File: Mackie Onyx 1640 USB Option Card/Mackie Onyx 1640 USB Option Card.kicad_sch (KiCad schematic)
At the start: 0 parts

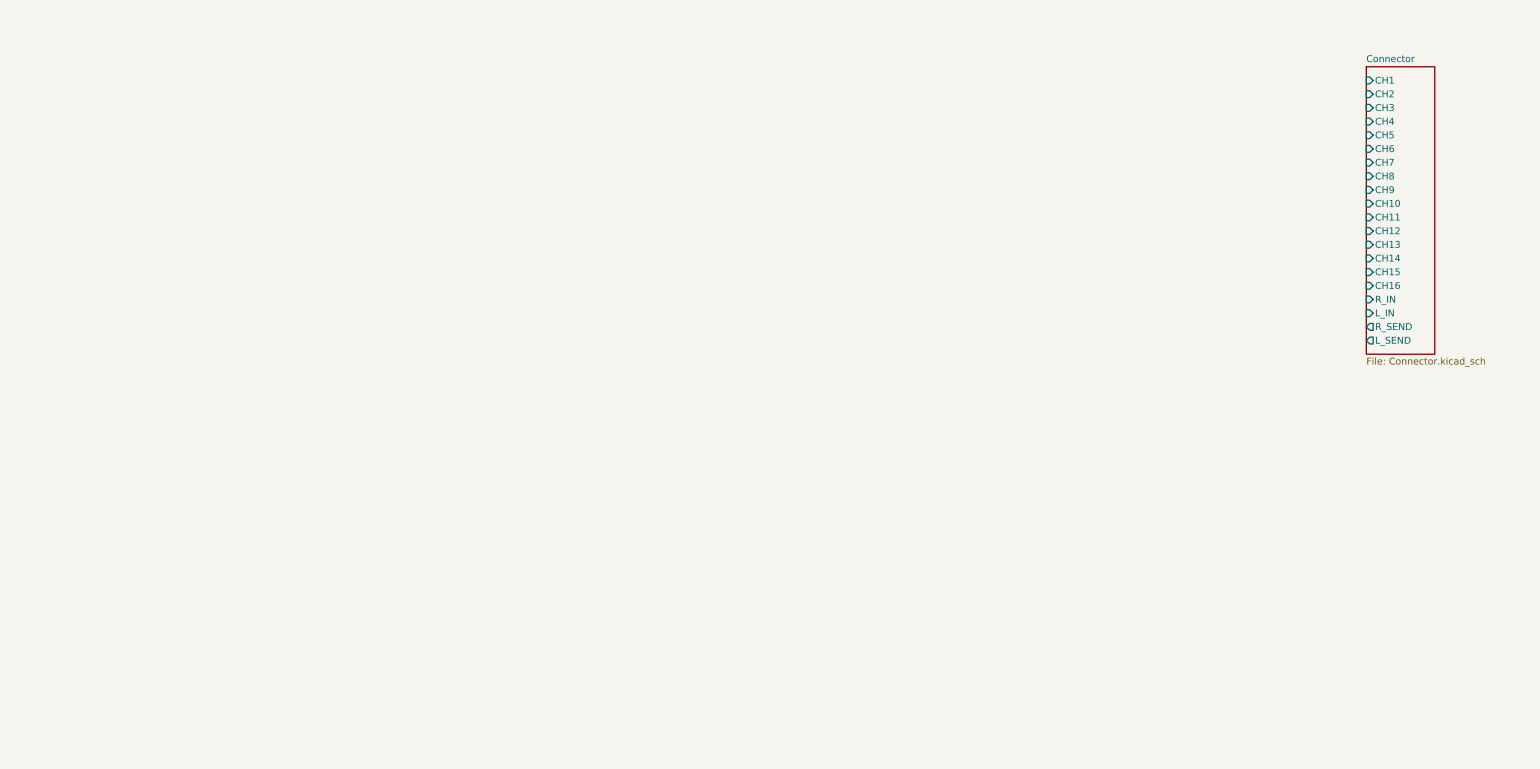
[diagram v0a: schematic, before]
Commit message: added XMOS XU316-1024-QF60B-C24 MCU (following footprint in pcb) started MCU power and usb phy implementation following datasheet
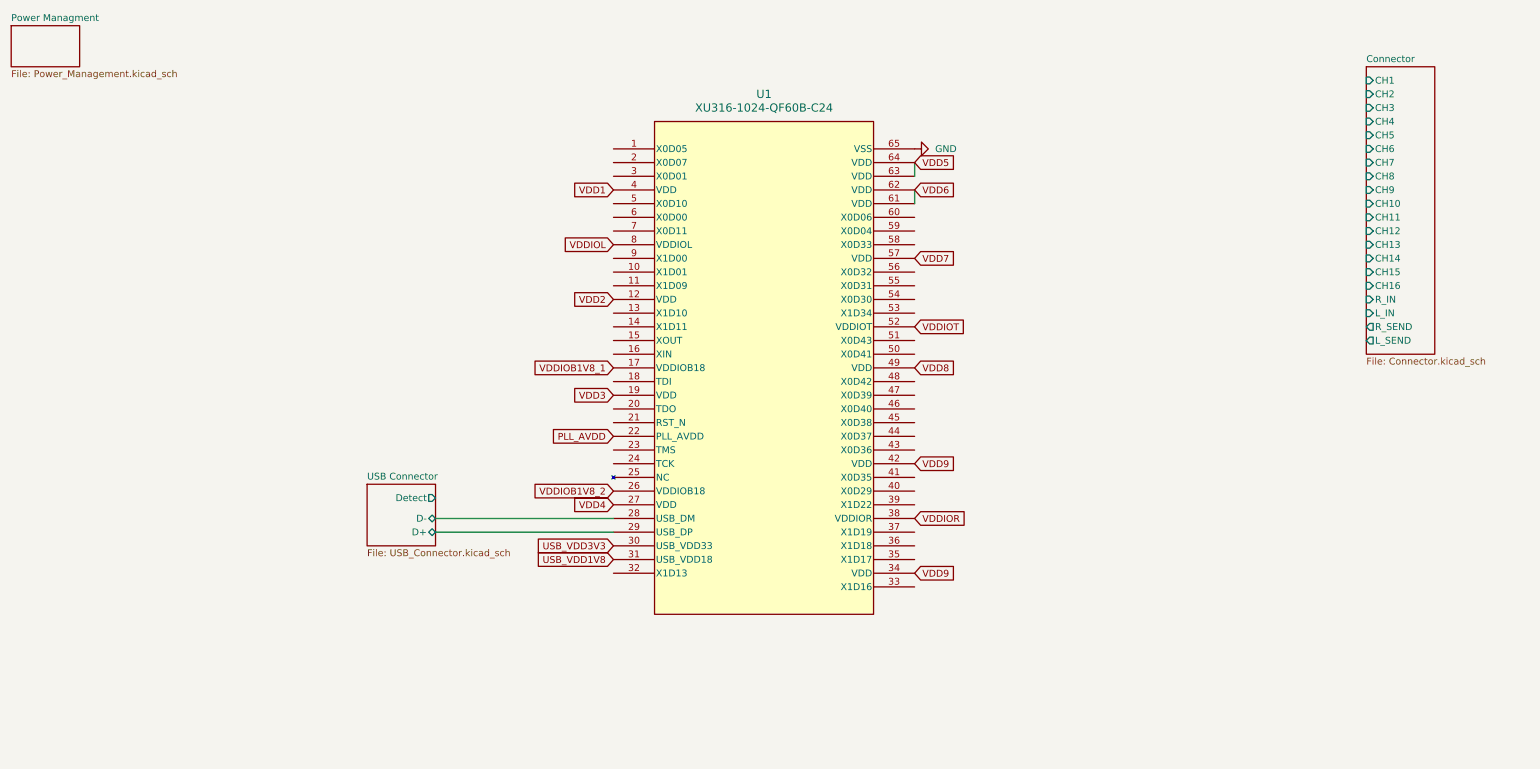
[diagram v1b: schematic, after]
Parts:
- added U1: XU316-1024-QF60B-C24, Package_DFN_QFN:QFN-60-1EP_7x7mm_P0.4mm_EP3.4x3.4mm_ThermalVias, symbol Mackie Onyx 1640 USB Option Card:XU316-1024-QF60B-C24
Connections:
- new net GND: U1.65 (VSS)
- new net PLL_AVDD: U1.22 (PLL_AVDD)
- new net USB Connector/D+: U1.29 (USB_DP)
- new net USB Connector/D-: U1.28 (USB_DM)
- new net USB_VDD1V8: U1.31 (USB_VDD18)
- new net USB_VDD3V3: U1.30 (USB_VDD33)
- new net VDD1: U1.4 (VDD)
- new net VDD2: U1.12 (VDD)
- new net VDD3: U1.19 (VDD)
- new net VDD4: U1.27 (VDD)
- new net VDD5: U1.63 (VDD), U1.64 (VDD)
- new net VDD6: U1.61 (VDD), U1.62 (VDD)
- new net VDD7: U1.57 (VDD)
- new net VDD8: U1.49 (VDD)
- new net VDD9: U1.34 (VDD), U1.42 (VDD)
- new net VDDIOB1V8_1: U1.17 (VDDIOB18)
- new net VDDIOB1V8_2: U1.26 (VDDIOB18)
- new net VDDIOL: U1.8 (VDDIOL)
- new net VDDIOR: U1.38 (VDDIOR)
- new net VDDIOT: U1.52 (VDDIOT)
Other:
- added sheet Power Managment (Power_Management.kicad_sch)
- added sheet USB Connector (USB_Connector.kicad_sch)

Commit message: Added a TI-TLV320 ADC Added power for ADC put the filter caps next to pins where they belong Added footprints for ADC and MCU
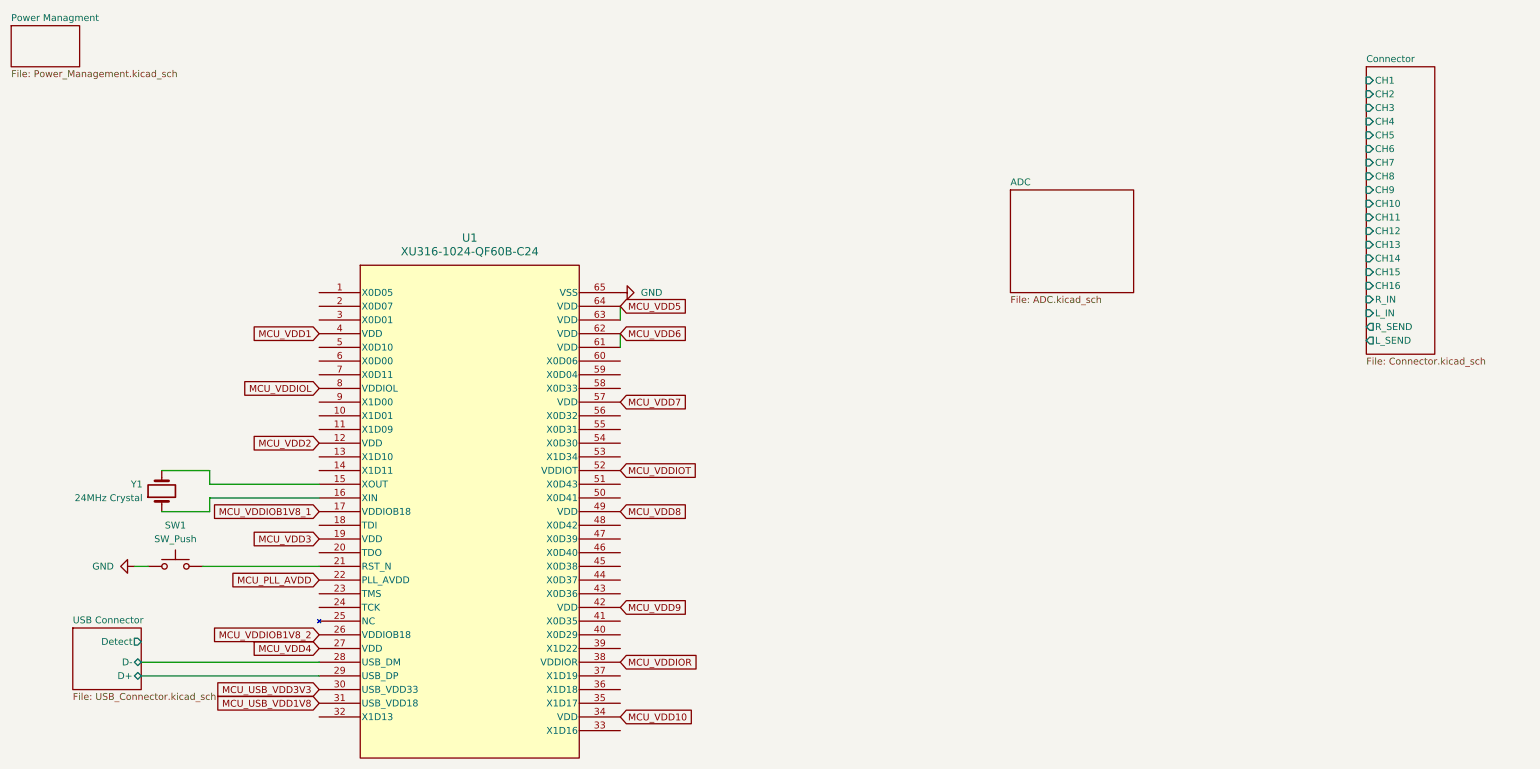
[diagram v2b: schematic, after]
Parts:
- added SW1: SW_Push, Button_Switch_THT:SW_PUSH_6mm, symbol Switch:SW_Push
- added Y1: 24MHz Crystal, Crystal:Crystal_HC49-U_Vertical, symbol Device:Crystal
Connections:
- net GND: now also SW1.1
- net at U1.15 (XOUT): now also Y1.2
- net at U1.16 (XIN): now also Y1.1
- net at U1.21 (RST_N): now also SW1.2
- net PLL_AVDD renamed MCU_PLL_AVDD
- net USB_VDD1V8 renamed MCU_USB_VDD1V8
- net USB_VDD3V3 renamed MCU_USB_VDD3V3
- net VDD1 renamed MCU_VDD1
- net VDD2 renamed MCU_VDD2
- net VDD3 renamed MCU_VDD3
- net VDD4 renamed MCU_VDD4
- net VDD5 renamed MCU_VDD5
- net VDD6 renamed MCU_VDD6
- net VDD7 renamed MCU_VDD7
- net VDD8 renamed MCU_VDD8
- net VDD9 renamed MCU_VDD10
- net MCU_VDD10: no longer U1.42 (VDD)
- net VDDIOB1V8_1 renamed MCU_VDDIOB1V8_1
- net VDDIOB1V8_2 renamed MCU_VDDIOB1V8_2
- net VDDIOL renamed MCU_VDDIOL
- net VDDIOR renamed MCU_VDDIOR
- net VDDIOT renamed MCU_VDDIOT
- new net MCU_VDD9: U1.42 (VDD)
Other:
- added sheet ADC (ADC.kicad_sch)
- moved on the sheet: U1

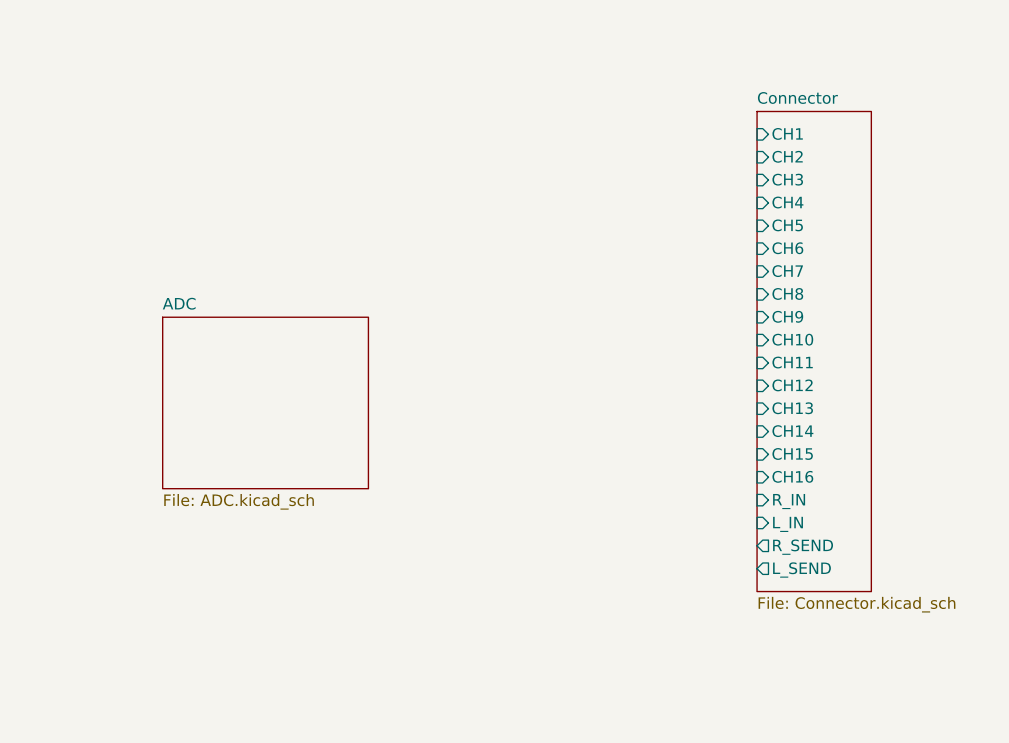
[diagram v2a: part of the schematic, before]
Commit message: Added Balancing Circuit ADC input is balanced, card connector isnt schematic following the one from original firewire card since ADC input voltage ratings are very close quad-op-amp-ic is placeholder with standard footprint, a higher quality one may be used on BOM did a bit of more or less rough PCB layouting
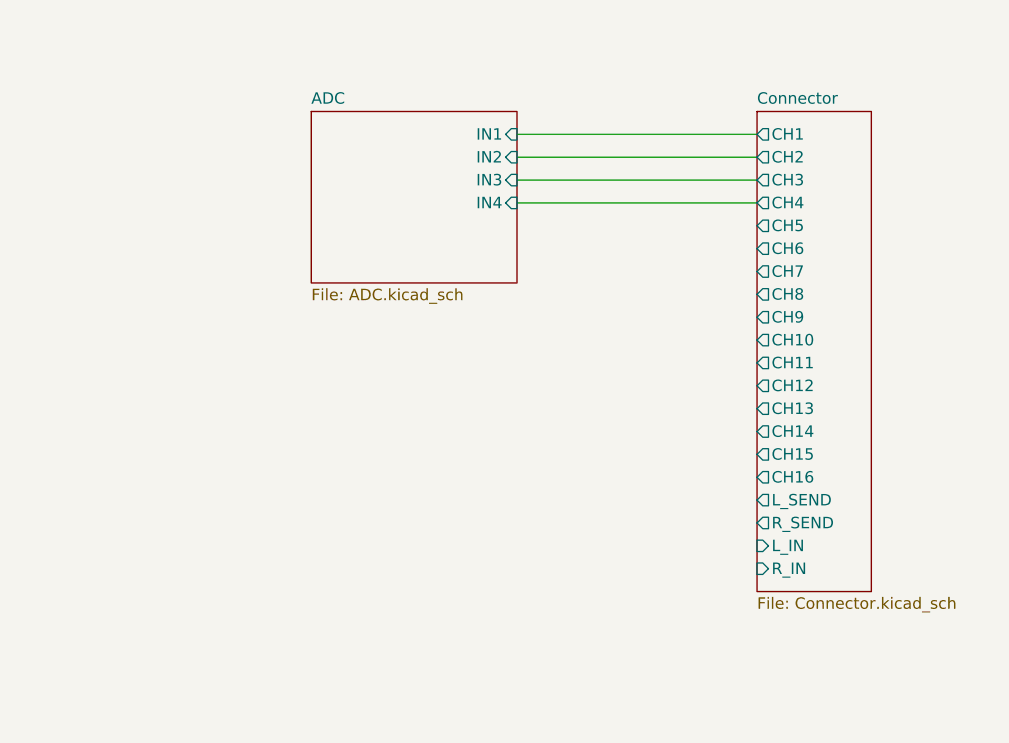
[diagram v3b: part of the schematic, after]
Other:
- sheet ADC ports: added IN1, IN2, IN3, IN4; removed none
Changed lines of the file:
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@@
+	(wire
+		(pts
+			(xy 241.3 35.56) (xy 267.97 35.56)
+		)
+		(stroke
+			(width 0)
+			(type default)
+		)
+	)
+	(wire
+		(pts
+			(xy 241.3 27.94) (xy 267.97 27.94)
+		)
+		(stroke
+			(width 0)
+			(type default)
+		)
+	)
 	(wire
 		(pts
@@
 	(wire
 		(pts
+			(xy 241.3 33.02) (xy 267.97 33.02)
+		)
+		(stroke
+			(width 0)
+			(type default)
+		)
+	)
+	(wire
+		(pts
 			(xy 39.37 118.11) (xy 41.91 118.11)
 		)
@@
 		(pts
 			(xy 40.64 138.43) (xy 73.66 138.43)
+		)
+		(stroke
+			(width 0)
+			(type default)
+		)
+	)
+	(wire
+		(pts
+			(xy 241.3 30.48) (xy 267.97 30.48)
 		)
 		(stroke
@@
 			)
 		)
-		(pin "CH1" input
+		(pin "CH4" output
+			(at 267.97 35.56 180)
+			(effects
+				(font
+					(size 1.27 1.27)
+				)
+				(justify left)
+			)
+		)
+		(pin "CH7" output
+			(at 267.97 43.18 180)
+			(effects
+				(font
+					(size 1.27 1.27)
+				)
+				(justify left)
+			)
+		)
+		(pin "CH2" output
+			(at 267.97 30.48 180)
+			(effects
+				(font
+					(size 1.27 1.27)
+				)
+				(justify left)
+			)
+		)
+		(pin "CH9" output
+			(at 267.97 48.26 180)
+			(effects
+				(font
+					(size 1.27 1.27)
+				)
+				(justify left)
+			)
+		)
+		(pin "CH1" output
 			(at 267.97 27.94 180)
 			(effects
@@
 			)
 		)
-		(pin "CH2" input
-			(at 267.97 30.48 180)
-			(effects
-				(font
-					(size 1.27 1.27)
-				)
-				(justify left)
-			)
-		)
-		(pin "CH4" input
-			(at 267.97 35.56 180)
-			(effects
-				(font
-					(size 1.27 1.27)
-				)
-				(justify left)
-			)
-		)
-		(pin "CH5" input
+		(pin "CH3" output
+			(at 267.97 33.02 180)
+			(effects
+				(font
+					(size 1.27 1.27)
+				)
+				(justify left)
+			)
+		)
+		(pin "CH6" output
+			(at 267.97 40.64 180)
+			(effects
+				(font
+					(size 1.27 1.27)
+				)
+				(justify left)
+			)
+		)
+		(pin "CH5" output
 			(at 267.97 38.1 180)
 			(effects
@@
 			)
 		)
-		(pin "CH7" input
-			(at 267.97 43.18 180)
-			(effects
-				(font
-					(size 1.27 1.27)
-				)
-				(justify left)
-			)
-		)
-		(pin "CH3" input
-			(at 267.97 33.02 180)
-			(effects
-				(font
-					(size 1.27 1.27)
-				)
-				(justify left)
-			)
-		)
-		(pin "CH8" input
+		(pin "CH8" output
 			(at 267.97 45.72 180)
 			(effects
@@
 			)
 		)
-		(pin "CH10" input
+		(pin "CH10" output
 			(at 267.97 50.8 180)
 			(effects
@@
 			)
 		)
-		(pin "CH12" input
+		(pin "CH11" output
+			(at 267.97 53.34 180)
+			(effects
+				(font
+					(size 1.27 1.27)
+				)
+				(justify left)
+			)
+		)
+		(pin "CH14" output
+			(at 267.97 60.96 180)
+			(effects
+				(font
+					(size 1.27 1.27)
+				)
+				(justify left)
+			)
+		)
+		(pin "CH13" output
+			(at 267.97 58.42 180)
+			(effects
+				(font
+					(size 1.27 1.27)
+				)
+				(justify left)
+			)
+		)
+		(pin "CH12" output
 			(at 267.97 55.88 180)
 			(effects
@@
 			)
 		)
-		(pin "CH6" input
-			(at 267.97 40.64 180)
-			(effects
-				(font
-					(size 1.27 1.27)
-				)
-				(justify left)
-			)
-		)
-		(pin "CH11" input
-			(at 267.97 53.34 180)
-			(effects
-				(font
-					(size 1.27 1.27)
-				)
-				(justify left)
-			)
-		)
-		(pin "CH9" input
-			(at 267.97 48.26 180)
-			(effects
-				(font
-					(size 1.27 1.27)
-				)
-				(justify left)
-			)
-		)
-		(pin "CH13" input
-			(at 267.97 58.42 180)
-			(effects
-				(font
-					(size 1.27 1.27)
-				)
-				(justify left)
-			)
-		)
-		(pin "CH15" input
+		(pin "CH16" output
+			(at 267.97 66.04 180)
+			(effects
+				(font
+					(size 1.27 1.27)
+				)
+				(justify left)
+			)
+		)
+		(pin "CH15" output
 			(at 267.97 63.5 180)
 			(effects
@@
 			)
 		)
-		(pin "CH14" input
-			(at 267.97 60.96 180)
+		(pin "L_IN" input
+			(at 267.97 73.66 180)
 			(effects
 				(font
@@
 		)
 		(pin "R_SEND" output
-			(at 267.97 73.66 180)
+			(at 267.97 71.12 180)
 			(effects
 				(font
@@
 		)
 		(pin "R_IN" input
+			(at 267.97 76.2 180)
+			(effects
+				(font
+					(size 1.27 1.27)
+				)
+				(justify left)
+			)
+		)
+		(pin "L_SEND" output
 			(at 267.97 68.58 180)
-			(effects
-				(font
-					(size 1.27 1.27)
-				)
-				(justify left)
-			)
-		)
-		(pin "L_IN" input
-			(at 267.97 71.12 180)
-			(effects
-				(font
-					(size 1.27 1.27)
-				)
-				(justify left)
-			)
-		)
-		(pin "L_SEND" output
-			(at 267.97 76.2 180)
-			(effects
-				(font
-					(size 1.27 1.27)
-				)
-				(justify left)
-			)
-		)
-		(pin "CH16" input
-			(at 267.97 66.04 180)
 			(effects
 				(font
@@
 	)
 	(sheet
-		(at 201.93 48.26)
+		(at 218.44 25.4)
 		(size 22.86 19.05)
 		(exclude_from_sim no)
@@
 		)
 		(property "Sheetname" "ADC"
-			(at 201.93 47.5484 0)
+			(at 218.44 24.6884 0)
 			(effects
 				(font
@@
 		)
 		(property "Sheetfile" "ADC.kicad_sch"
-			(at 201.93 67.8946 0)
+			(at 218.44 45.0346 0)
 			(effects
 				(font
@@
 			)
 		)
+		(pin "IN1" input
+			(at 241.3 27.94 0)
+			(effects
+				(font
+					(size 1.27 1.27)
+				)
+				(justify right)
+			)
+		)
+		(pin "IN2" input
+			(at 241.3 30.48 0)
+			(effects
+				(font
+					(size 1.27 1.27)
+				)
+				(justify right)
+			)
+		)
+		(pin "IN3" input
+			(at 241.3 33.02 0)
+			(effects
+				(font
+					(size 1.27 1.27)
+				)
+				(justify right)
+			)
+		)
+		(pin "IN4" input
+			(at 241.3 35.56 0)
+			(effects
+				(font
+					(size 1.27 1.27)
+				)
+				(justify right)
+			)
+		)
